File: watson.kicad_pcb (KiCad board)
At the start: 2 copper layers, 133.3 x 77.2 mm, 37 parts, among them P1 CONN_1, P2 CONN_1, P3 CONN_1, P4 CONN_1, P5 BNC, P6 CONN_1, U4 AD603

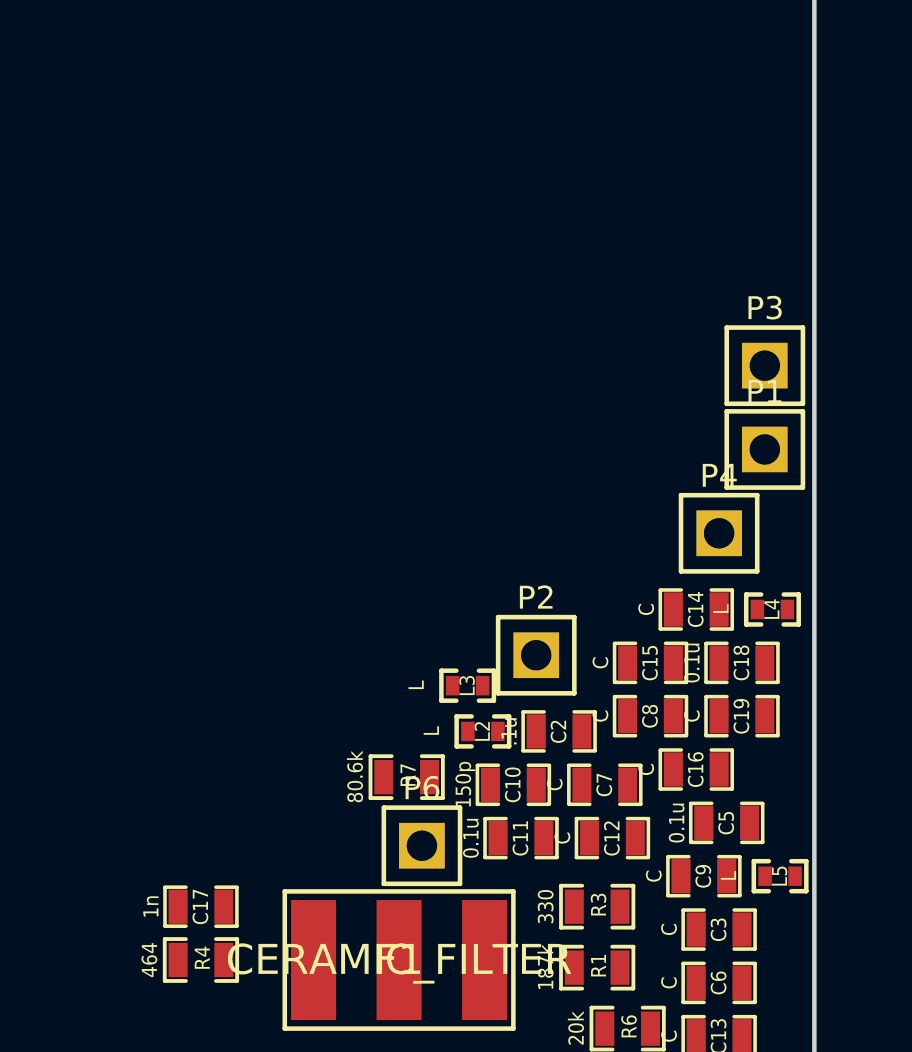
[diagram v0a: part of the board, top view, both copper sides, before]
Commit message: Added footprints SOT89, c_tant_A, AD8307; Added new footprint parts to pcb.
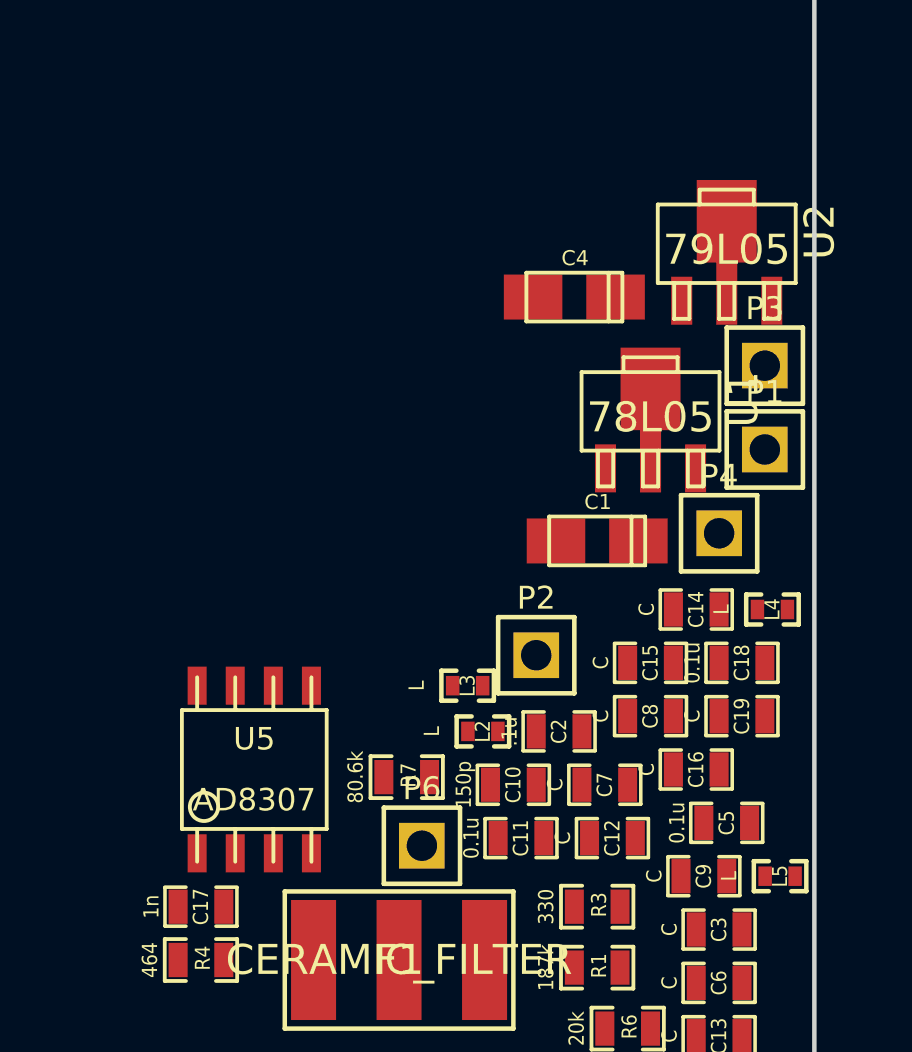
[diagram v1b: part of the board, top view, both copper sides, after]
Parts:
- added C1: 33u, c_tant_A, F.Cu at (268.0, 137.9)
- added C4: 33u, c_tant_A, F.Cu at (267.2, 129.8)
- added U1: 78L05, sot89, F.Cu at (269.7, 133.6)
- added U2: 79L05, sot89, F.Cu at (272.3, 128.0)
- added U5: AD8307, AD8307, F.Cu at (256.5, 145.5)

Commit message: Added chip coil layout
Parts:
- added L1: 750nH, 180mm_ChipCoil, F.Cu at (253.7, 134.5)
- added RV1: 5k, VRSM3932_JHOOK, F.Cu at (261.9, 136.1)
- U4: footprint AD603 -> so-8
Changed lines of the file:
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@@
 (kicad_pcb (version 3) (host pcbnew "(2013-mar-25)-stable")
   (general
-    (links 76)
-    (no_connects 74)
-    (area 141.732 91.694 275.336 169.164)
+    (links 81)
+    (no_connects 79)
+    (area 141.783999 91.872999 275.284001 169.239001)
     (thickness 1.6)
     (drawings 4)
     (tracks 0)
     (zones 0)
-    (modules 42)
+    (modules 44)
     (nets 22)
   )
@@
     (mod_text_size 1 1)
     (mod_text_width 0.15)
-    (pad_size 1 1)
-    (pad_drill 0.6)
+    (pad_size 0.75 2.65)
+    (pad_drill 0)
     (pad_to_mask_clearance 0)
     (aux_axis_origin 0 0)
@@
     )
   )
-  (module AD603 (layer F.Cu)
-    (at 269.748 163.068)
-    (descr "SMD-8 Surface Mount 300mil 8pin Dual In Line Package")
-    (tags "Power Integrations G Package")
-    (fp_text reference U4 (at 0 0 90) (layer F.SilkS)
-      (effects (font (size 1.524 1.524) (thickness 0.3048)))
-    )
-    (fp_text value AD603 (at 0 0) (layer F.SilkS) hide
-      (effects (font (size 1.524 1.524) (thickness 0.3048)))
-    )
-    (fp_line (start 2.413 3.302) (end 2.667 3.302) (layer F.SilkS) (width 0.381))
-    (fp_line (start -0.127 3.302) (end 0.127 3.302) (layer F.SilkS) (width 0.381))
-    (fp_line (start -2.667 3.302) (end -2.413 3.302) (layer F.SilkS) (width 0.381))
-    (fp_line (start -2.667 -3.302) (end -2.413 -3.302) (layer F.SilkS) (width 0.381))
-    (fp_line (start -0.127 -3.302) (end 0.127 -3.302) (layer F.SilkS) (width 0.381))
-    (fp_line (start 2.413 -3.302) (end 2.667 -3.302) (layer F.SilkS) (width 0.381))
-    (fp_circle (center -4.064 2.159) (end -3.81 2.159) (layer F.SilkS) (width 0.381))
-    (fp_line (start -5.08 1.016) (end -5.08 3.302) (layer F.SilkS) (width 0.381))
-    (fp_line (start -5.08 -3.302) (end -5.08 -1.016) (layer F.SilkS) (width 0.381))
-    (fp_arc (start -5.08 0) (end -4.064 0) (angle 90) (layer F.SilkS) (width 0.381))
-    (fp_arc (start -5.08 0) (end -5.08 -1.016) (angle 90) (layer F.SilkS) (width 0.381))
-    (fp_line (start 5.08 -3.302) (end 4.572 -3.302) (layer F.SilkS) (width 0.381))
-    (fp_line (start 5.08 3.302) (end 4.572 3.302) (layer F.SilkS) (width 0.381))
-    (fp_line (start -5.08 3.302) (end -4.572 3.302) (layer F.SilkS) (width 0.381))
-    (fp_line (start -5.08 -3.302) (end -4.572 -3.302) (layer F.SilkS) (width 0.381))
-    (fp_line (start 5.08 -3.302) (end 5.08 3.302) (layer F.SilkS) (width 0.381))
-    (pad 1 smd rect (at -3.6322 4.318) (size 1.1684 2.032)
-      (layers F.Cu F.Paste F.Mask)
-      (net 3 /GPOS)
-    )
-    (pad 2 smd rect (at -1.27 4.318) (size 1.524 2.032)
-      (layers F.Cu F.Paste F.Mask)
-      (net 16 N-0000016)
-    )
-    (pad 3 smd rect (at 1.27 4.318) (size 1.524 2.032)
-      (layers F.Cu F.Paste F.Mask)
-      (net 18 N-0000021)
-    )
-    (pad 4 smd rect (at 3.6322 4.318) (size 1.1684 2.032)
-      (layers F.Cu F.Paste F.Mask)
-      (net 9 GND)
-    )
-    (pad 5 smd rect (at 3.6322 -4.318) (size 1.1684 2.032)
-      (layers F.Cu F.Paste F.Mask)
-      (net 21 N-000008)
-    )
-    (pad 6 smd rect (at 1.27 -4.318) (size 1.524 2.032)
-      (layers F.Cu F.Paste F.Mask)
-      (net 6 /VNEG)
-    )
-    (pad 7 smd rect (at -1.27 -4.318) (size 1.524 2.032)
-      (layers F.Cu F.Paste F.Mask)
-      (net 20 N-000007)
-    )
-    (pad 8 smd rect (at -3.6322 -4.318) (size 1.1684 2.032)
-      (layers F.Cu F.Paste F.Mask)
-      (net 7 /VPOS)
-    )
-  )
   (module sot89   placed (layer F.Cu)
     (at 272.288 128.016)
@@
       (rotate (xyz 0 0 0))
     )
+  )
+  (module VRSM3932_JHOOK (layer F.Cu)
+    (at 261.874 136.144)
+    (fp_text reference RV1 (at 0 0) (layer F.SilkS)
+      (effects (font (size 1 1) (thickness 0.15)))
+    )
+    (fp_text value 5k (at -0.254 1.524) (layer F.SilkS)
+      (effects (font (size 1 1) (thickness 0.15)))
+    )
+    (fp_circle (center 1.143 1.8415) (end 1.2065 1.524) (layer F.SilkS) (width 0.1))
+    (fp_line (start -1.75 -2.4) (end 1.75 -2.4) (layer F.SilkS) (width 0.1))
+    (fp_line (start 1.75 -2.4) (end 1.75 2.4) (layer F.SilkS) (width 0.1))
+    (fp_line (start -1.75 2.4) (end 1.75 2.4) (layer F.SilkS) (width 0.1))
+    (fp_line (start -1.75 2.4) (end -1.75 -2.4) (layer F.SilkS) (width 0.1))
+    (pad 1 smd rect (at -1.45 -1.27) (size 1.6 1.3)
+      (layers F.Cu F.Paste F.Mask)
+      (net 21 N-000008)
+    )
+    (pad 3 smd rect (at -1.45 1.27) (size 1.6 1.3)
+      (layers F.Cu F.Paste F.Mask)
+      (net 20 N-000007)
+    )
+    (pad 2 smd rect (at 1.45 0) (size 1.6 2)
+      (layers F.Cu F.Paste F.Mask)
+      (net 21 N-000008)
+    )
+  )
+  (module so-8 (layer F.Cu)
+    (at 269.748 163.068)
+    (descr SO-8)
+    (attr smd)
+    (fp_text reference U4 (at 0 -1.016) (layer F.SilkS)
+      (effects (font (size 0.7493 0.7493) (thickness 0.14986)))
+    )
+    (fp_text value AD603 (at 0 1.016) (layer F.SilkS)
+      (effects (font (size 0.7493 0.7493) (thickness 0.14986)))
+    )
+    (fp_line (start -2.413 -1.9812) (end -2.413 1.9812) (layer F.SilkS) (width 0.127))
+    (fp_line (start -2.413 1.9812) (end 2.413 1.9812) (layer F.SilkS) (width 0.127))
+    (fp_line (start 2.413 1.9812) (end 2.413 -1.9812) (layer F.SilkS) (width 0.127))
+    (fp_line (start 2.413 -1.9812) (end -2.413 -1.9812) (layer F.SilkS) (width 0.127))
+    (fp_line (start -1.905 -1.9812) (end -1.905 -3.0734) (layer F.SilkS) (width 0.127))
+    (fp_line (start -0.635 -1.9812) (end -0.635 -3.0734) (layer F.SilkS) (width 0.127))
+    (fp_line (start 0.635 -1.9812) (end 0.635 -3.0734) (layer F.SilkS) (width 0.127))
+    (fp_line (start 1.905 -3.0734) (end 1.905 -1.9812) (layer F.SilkS) (width 0.127))
+    (fp_line (start 1.905 1.9812) (end 1.905 3.0734) (layer F.SilkS) (width 0.127))
+    (fp_line (start 0.635 3.0734) (end 0.635 1.9812) (layer F.SilkS) (width 0.127))
+    (fp_line (start -0.635 3.0734) (end -0.635 1.9812) (layer F.SilkS) (width 0.127))
+    (fp_line (start -1.905 3.0734) (end -1.905 1.9812) (layer F.SilkS) (width 0.127))
+    (fp_circle (center -1.6764 1.2446) (end -1.9558 1.6256) (layer F.SilkS) (width 0.127))
+    (pad 1 smd rect (at -1.905 2.794) (size 0.635 1.27)
+      (layers F.Cu F.Paste F.Mask)
+      (net 3 /GPOS)
+    )
+    (pad 2 smd rect (at -0.635 2.794) (size 0.635 1.27)
+      (layers F.Cu F.Paste F.Mask)
+      (net 16 N-0000016)
+    )
+    (pad 3 smd rect (at 0.635 2.794) (size 0.635 1.27)
+      (layers F.Cu F.Paste F.Mask)
+      (net 18 N-0000021)
+    )
+    (pad 4 smd rect (at 1.905 2.794) (size 0.635 1.27)
+      (layers F.Cu F.Paste F.Mask)
+      (net 9 GND)
+    )
+    (pad 5 smd rect (at 1.905 -2.794) (size 0.635 1.27)
+      (layers F.Cu F.Paste F.Mask)
+      (net 21 N-000008)
+    )
+    (pad 6 smd rect (at 0.635 -2.794) (size 0.635 1.27)
+      (layers F.Cu F.Paste F.Mask)
+      (net 6 /VNEG)
+    )
+    (pad 7 smd rect (at -0.635 -2.794) (size 0.635 1.27)
+      (layers F.Cu F.Paste F.Mask)
+      (net 20 N-000007)
+    )
+    (pad 8 smd rect (at -1.905 -2.794) (size 0.635 1.27)
+      (layers F.Cu F.Paste F.Mask)
+      (net 7 /VPOS)
+    )
+    (model smd/smd_dil/so-8.wrl
+      (at (xyz 0 0 0))
+      (scale (xyz 1 1 1))
+      (rotate (xyz 0 0 0))
+    )
+  )
+  (module 180mm_ChipCoil (layer F.Cu)
+    (at 253.746 134.493)
+    (attr smd)
+    (fp_text reference L1 (at 0 0 90) (layer F.SilkS)
+      (effects (font (size 0.50038 0.4572) (thickness 0.1143)))
+    )
+    (fp_text value 750nH (at -1.69926 0 90) (layer F.SilkS)
+      (effects (font (size 0.508 0.4572) (thickness 0.1143)))
+    )
+    (fp_line (start -0.375 -0.5) (end -0.875 -0.5) (layer F.SilkS) (width 0.15))
+    (fp_line (start -0.875 -0.5) (end -0.875 0.5) (layer F.SilkS) (width 0.15))
+    (fp_line (start -0.875 0.5) (end -0.375 0.5) (layer F.SilkS) (width 0.15))
+    (fp_line (start 0.375 -0.5) (end 0.875 -0.5) (layer F.SilkS) (width 0.15))
+    (fp_line (start 0.875 -0.5) (end 0.875 0.5) (layer F.SilkS) (width 0.15))
+    (fp_line (start 0.875 0.5) (end 0.375 0.5) (layer F.SilkS) (width 0.15))
+    (pad 1 smd rect (at -0.95 0) (size 0.75 2.65)
+      (layers F.Cu F.Paste F.Mask)
+      (net 19 N-000004)
+    )
+    (pad 2 smd rect (at 0.95 0) (size 0.75 2.65)
+      (layers F.Cu F.Paste F.Mask)
+      (net 18 N-0000021)
+    )
+    (model smd\resistors\R0603.wrl
+      (at (xyz 0 0 0.001))
+      (scale (xyz 0.5 0.5 0.5))
+      (rotate (xyz 0 0 0))
+    )

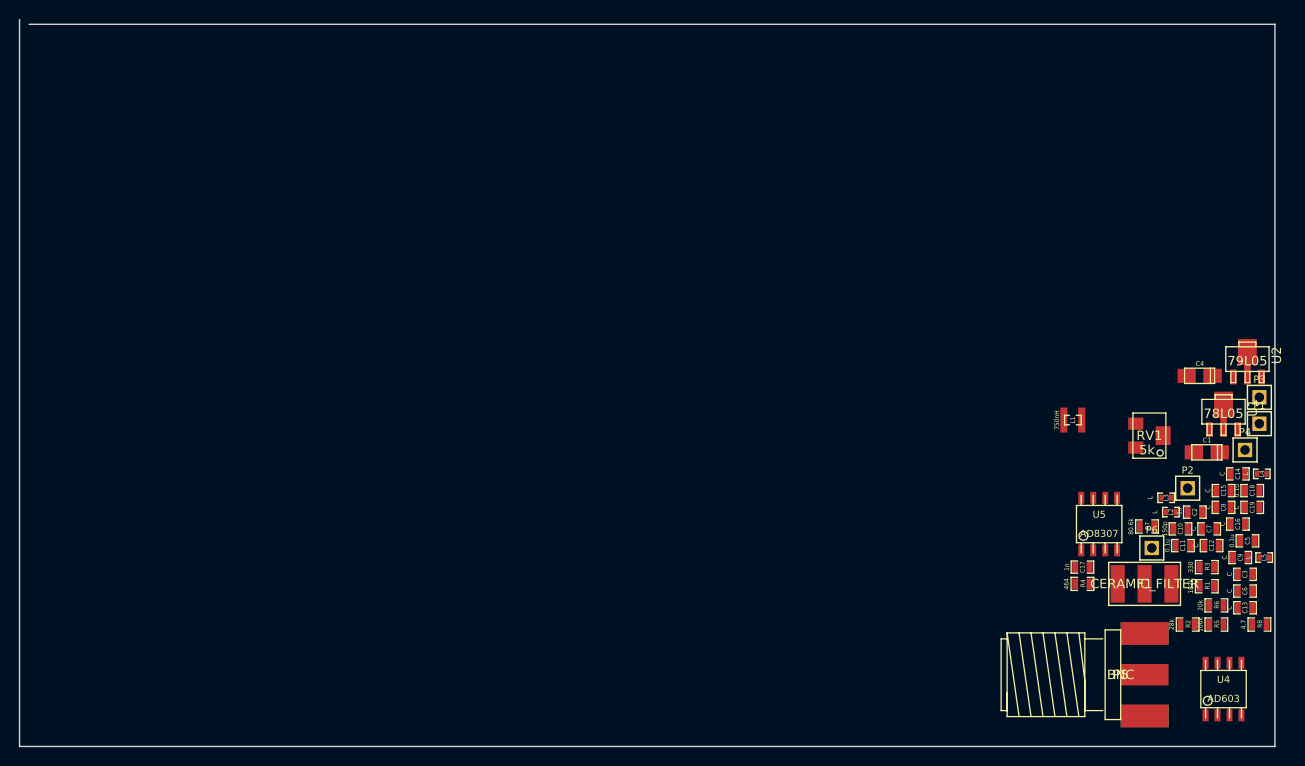
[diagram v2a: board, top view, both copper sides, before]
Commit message: Added AD8031 to buffer output of AD8307.
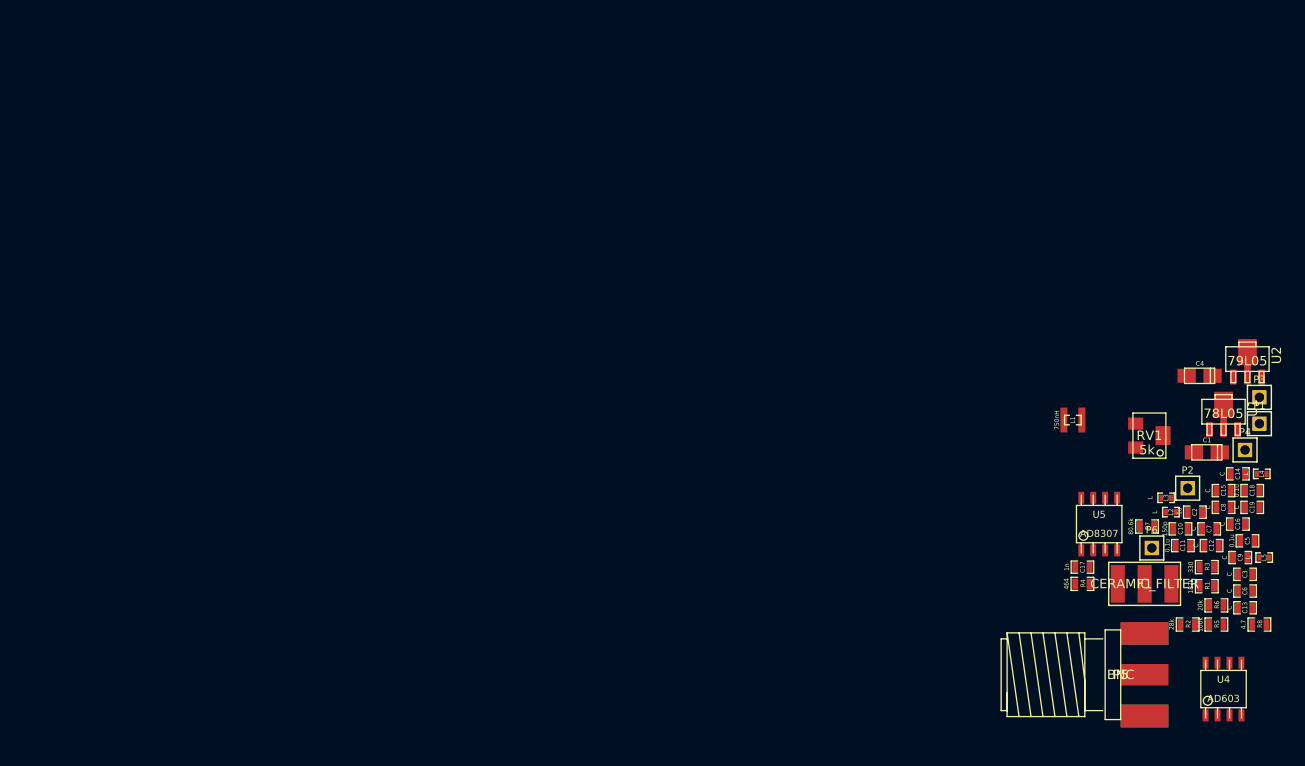
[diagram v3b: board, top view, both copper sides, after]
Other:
- board outline removed
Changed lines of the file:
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@@
     (links 81)
     (no_connects 79)
-    (area 141.783999 91.872999 275.284001 169.239001)
+    (area 245.821999 125.312484 276.4282 168.991482)
     (thickness 1.6)
-    (drawings 4)
+    (drawings 0)
     (tracks 0)
     (zones 0)
@@
     )
   )
-  (gr_line (start 141.859 169.164) (end 141.859 91.948) (angle 90) (layer Edge.Cuts) (width 0.15))
-  (gr_line (start 275.209 169.164) (end 141.859 169.164) (angle 90) (layer Edge.Cuts) (width 0.15))
-  (gr_line (start 275.209 92.456) (end 275.209 169.164) (angle 90) (layer Edge.Cuts) (width 0.15))
-  (gr_line (start 142.875 92.456) (end 275.209 92.456) (angle 90) (layer Edge.Cuts) (width 0.15))
 )

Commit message: This is the initial manufactured version of Watson, Watson 10 to be exact.
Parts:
- added C20: 0.1u, SM0603_Capa, F.Cu at (208.9, 136.8)
- added C21: 0.1u, SM0603_Capa, F.Cu at (210.8, 136.8)
- added C22: 1n, SM0603_Capa, F.Cu at (202.5, 140.6)
- added L6: L, SM0603_Inductor, F.Cu at (206.8, 135.3)
- added R10: R, SM0603_Resistor, F.Cu at (205.7, 141.7)
- added R9: R, SM0603_Resistor, F.Cu at (205.7, 143.8)
- added U3: AD8031, sot23, F.Cu at (205.8, 138.9)
- F1: value CERAMIC_FILTER -> BPF; footprint Murata_SFECV_Ceramic_Filter -> SFEC
- L2, L3, L4, L5: footprint SM0402_Inductor -> SM0603_Inductor
- moved P5 106.2 mm to (155.2, 138.2)
- moved C9 104.6 mm to (167.8, 135.6), turned to 270 degrees
- moved R5 104.0 mm to (167.8, 132.5), turned to 270 degrees
- moved R6 101.7 mm to (169.7, 132.5), turned to 270 degrees
- moved C8 100.4 mm to (169.7, 135.6), turned to 270 degrees
- moved U4 97.9 mm to (175.3, 137.5), turned to 270 degrees
- moved C10 97.7 mm to (167.8, 138.9), turned to 270 degrees
- moved R2 97.3 mm to (171.6, 132.5), turned to 270 degrees
- moved L4 95.9 mm to (178.1, 145.8), turned to 90 degrees
- moved C7 95.7 mm to (173.5, 132.5), turned to 90 degrees
- moved C13 95.7 mm to (177.3, 141.2), turned to 180 degrees
- moved R1 94.7 mm to (175.4, 132.5), turned to 90 degrees
- moved C14 94.0 mm to (177.3, 143.3), turned to 180 degrees
- moved R7 93.4 mm to (169.7, 129.3), turned to 90 degrees
- moved L5 90.7 mm to (184.9, 132.5), turned to 90 degrees
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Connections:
- F1 pad 3: N-0000015 -> (no net)
- P6 pad 1: N-0000020 -> N-0000017
- R4 pad 2: N-0000015 -> N-000003
- R6 pad 1: N-0000020 -> N-000001
- R7 pad 1: N-0000020 -> N-000001
- U5 pad 8: N-0000015 -> N-000003
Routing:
- net GND: track 0.00 -> 592.3 mm, vias 0 -> 341
- net +5V: track 0.00 -> 76.8 mm, vias 0 -> 5
- net -5V: track 0.00 -> 62.3 mm, vias 0 -> 2
- net N-0000019: track 0.00 -> 42.7 mm
- net N-0000017: track 0.00 -> 17.2 mm, vias 0 -> 2
- net N-0000011: track 0.00 -> 15.4 mm
- net N-0000010: track 0.00 -> 9.74 mm
- net N-000005: track 0.00 -> 9.69 mm
- net /V+: track 0.00 -> 8.93 mm
- net /V-: track 0.00 -> 8.38 mm
- net /VPS: track 0.00 -> 8.22 mm
- net /VNEG: track 0.00 -> 6.86 mm, vias 0 -> 2
- net /VPOS: track 0.00 -> 6.70 mm
- net /GPOS: track 0.00 -> 6.64 mm
- net N-0000026: track 0.00 -> 6.60 mm
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- added copper zone on B.Cu, net GND
- added copper zone on F.Cu, net GND
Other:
- board outline added: 84 x 30 mm
- net class 10 added: clearance 0.254, trace_width 0.254, via_dia 0.889, via_drill 0.635
- net class 20 added: clearance 0.254, trace_width 0.508, via_dia 0.889, via_drill 0.635
- net class 30 added: clearance 0.254, trace_width 0.762, via_dia 0.889, via_drill 0.635
- net class Default: trace_width 0.254 -> 0.508; via_dia 0.889 -> 0.6858; via_drill 0.635 -> 0.3302
- rule trace_min: 0.254 -> 0.1524
- rule via_min_drill: 0.508 -> 0.3302
- rule via_min_size: 0.889 -> 0.6858
